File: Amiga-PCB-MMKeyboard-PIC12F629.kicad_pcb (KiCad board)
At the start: 2 copper layers, 47.3 x 23.2 mm, 13 parts, among them J11 Amiga keyboard, J12 A500 mainboard, J2 PS/2 keyboard, SW500 SW_Push, U1 PIC12F629

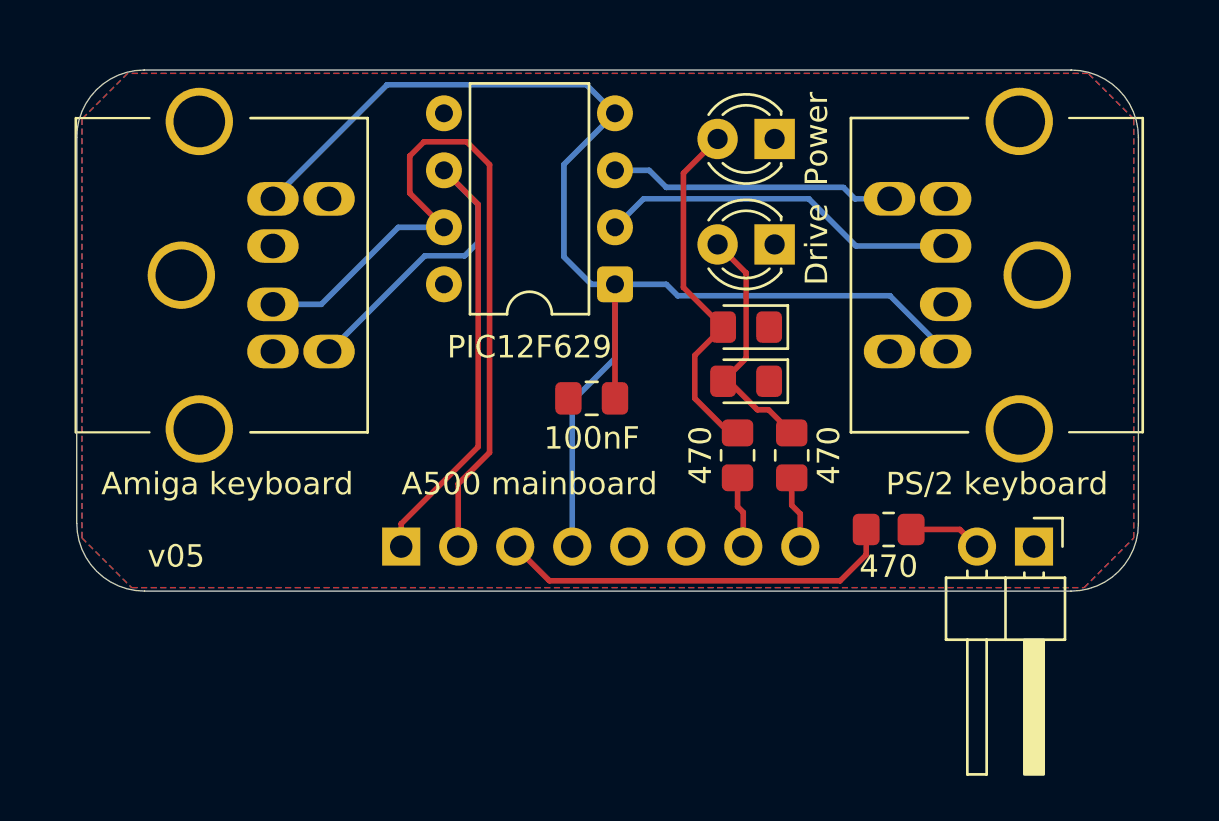
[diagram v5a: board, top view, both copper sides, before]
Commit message: v06: Sane LED resistor values depending on the LED's properties
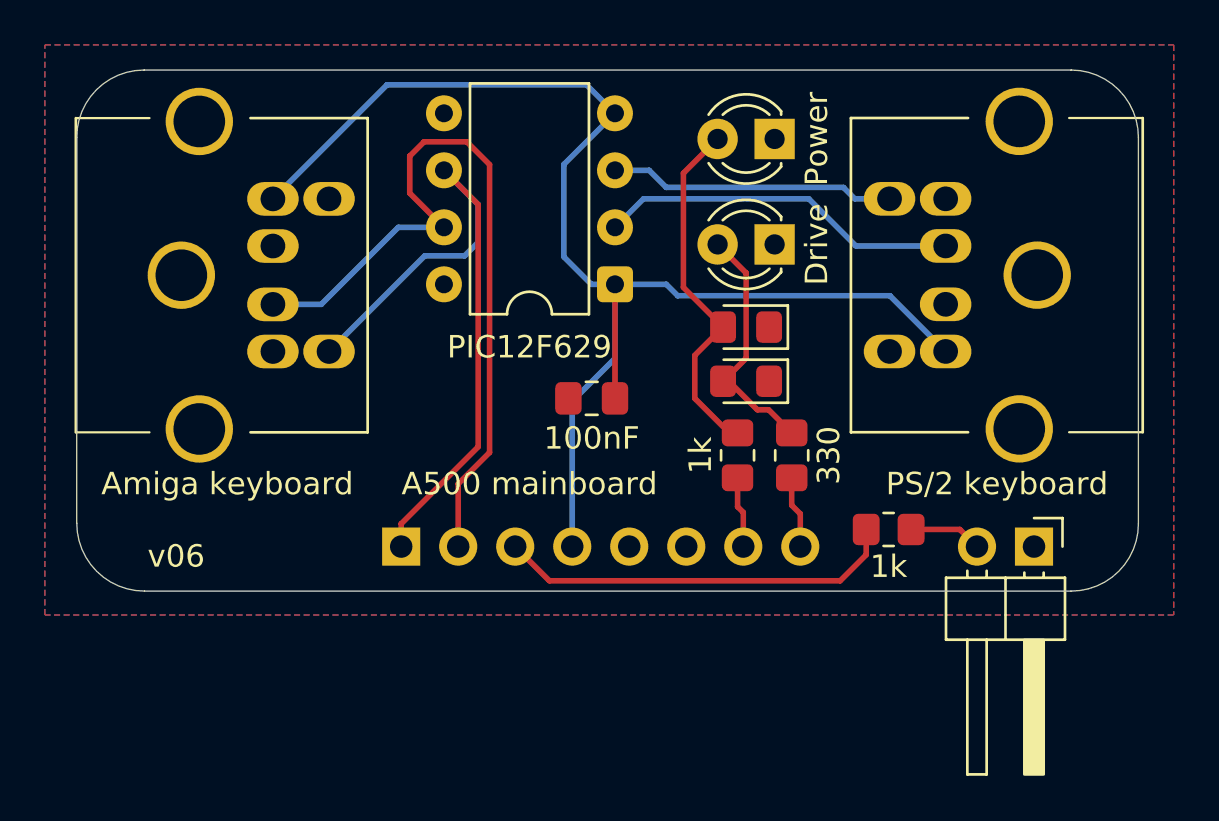
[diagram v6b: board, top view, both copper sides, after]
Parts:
- R1, R500: value 470 -> 1k
- R2: value 470 -> 330
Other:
- board text added: "v06"
- board text removed: "v05"
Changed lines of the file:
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@@
 			)
 		)
-		(property "Datasheet" ""
+		(property "Datasheet" "http://service.powerdynamics.com/ec/Catalog17/Section%2011.pdf"
 			(at 0 0 270)
 			(layer "F.Fab")
@@
 			)
 		)
-		(property "Description" "6-pin Mini-DIN connector"
+		(property "Description" ""
 			(at 0 0 270)
 			(layer "F.Fab")
@@
 			)
 		)
+		(property ki_fp_filters "MINI?DIN*")
+		(sheetname "/")
 		(sheetfile "Amiga-PCB-MMKeyboard-PIC12F629.kicad_sch")
 		(attr through_hole)
@@
 			)
 		)
-		(property "Description" "Light emitting diode"
+		(property "Description" ""
 			(at 0 0 180)
 			(layer "F.Fab")
@@
 			)
 		)
+		(property ki_fp_filters "LED* LED_SMD:* LED_THT:*")
+		(sheetname "/")
 		(sheetfile "Amiga-PCB-MMKeyboard-PIC12F629.kicad_sch")
 		(attr through_hole)
@@
 			)
 		)
-		(property "Value" "470"
+		(property "Value" "330"
 			(at 0 1.651 90)
 			(layer "F.SilkS")
@@
 			)
 		)
-		(property "Description" "Resistor"
+		(property "Description" ""
 			(at 0 0 90)
 			(layer "F.Fab")
@@
 			)
 		)
-		(property "JLCPCB" "C17710"
+		(property "JLCPCB" "C17630"
 			(at 243.586 -41.402 0)
 			(layer "F.Fab")
@@
 			)
 		)
-		(property "Reichelt" "SMD-0805 470"
+		(property "Reichelt" "SMD-0805 330"
 			(at 243.586 -41.402 0)
 			(layer "F.Fab")
@@
 			)
 		)
+		(property ki_fp_filters "R_*")
+		(sheetname "/")
 		(sheetfile "Amiga-PCB-MMKeyboard-PIC12F629.kicad_sch")
 		(attr smd)
@@
 			)
 		)
-		(property "Description" "Light emitting diode"
+		(property "Description" ""
 			(at 0 0 180)
 			(layer "F.Fab")
@@
 			)
 		)
+		(property ki_fp_filters "LED* LED_SMD:* LED_THT:*")
+		(sheetname "/")
 		(sheetfile "Amiga-PCB-MMKeyboard-PIC12F629.kicad_sch")
 		(attr smd)
@@
 			)
 		)
-		(property "Value" "470"
+		(property "Value" "1k"
 			(at 0 1.65 0)
 			(layer "F.SilkS")
@@
 			)
 		)
-		(property "Description" "Resistor"
+		(property "Description" ""
 			(at 0 0 0)
 			(layer "F.Fab")
@@
 			)
 		)
-		(property "JLCPCB" "C17710"
+		(property "JLCPCB" "C17513"
 			(at 0 0 0)
 			(layer "F.Fab")
@@
 			)
 		)
-		(property "Reichelt" "SMD-0805 470"
+		(property "Reichelt" "SMD-0805 1,00K"
 			(at 0 0 0)
 			(layer "F.Fab")
@@
 			)
 		)
+		(property ki_fp_filters "R_*")
+		(sheetname "/")
 		(sheetfile "Amiga-PCB-MMKeyboard-PIC12F629.kicad_sch")
 		(attr smd)
@@
 			)
 		)
-		(property "Description" "Push button switch, generic, two pins"
+		(property "Description" ""
 			(at 0 0 270)
 			(layer "F.Fab")
@@
 			)
 		)
+		(property "LCSC" "C7501290"
+			(at 0 0 270)
+			(unlocked yes)
+			(layer "F.Fab")
+			(hide yes)
+			(effects
+				(font
+					(size 1 1)
+					(thickness 0.15)
+				)
+			)
+		)
+		(property "Reichelt" "W+P 946-142"
+			(at 0 0 270)
+			(unlocked yes)
+			(layer "F.Fab")
+			(hide yes)
+			(effects
+				(font
+					(size 1 1)
+					(thickness 0.15)
+				)
+			)
+		)
+		(sheetname "/")
 		(sheetfile "Amiga-PCB-MMKeyboard-PIC12F629.kicad_sch")
 		(attr through_hole)
@@
 			)
 		)
-		(property "Datasheet" ""
+		(property "Datasheet" "http://ww1.microchip.com/downloads/en/DeviceDoc/41190G.pdf"
 			(at 0 0 180)
 			(layer "F.Fab")
@@
 			)
 		)
-		(property "Description" "1024W Flash, 64B SRAM, 128B EEPROM, PDIP8"
+		(property "Description" ""
 			(at 0 0 180)
 			(layer "F.Fab")
@@
 			)
 		)
+		(property ki_fp_filters "DIP*W7.62mm*")
+		(sheetname "/")
 		(sheetfile "Amiga-PCB-MMKeyboard-PIC12F629.kicad_sch")
 		(attr through_hole)
@@
 			)
 		)
-		(property "Description" "Light emitting diode"
+		(property "Description" ""
 			(at 0 0 180)
 			(layer "F.Fab")
@@
 			)
 		)
+		(property ki_fp_filters "LED* LED_SMD:* LED_THT:*")
+		(sheetname "/")
 		(sheetfile "Amiga-PCB-MMKeyboard-PIC12F629.kicad_sch")
 		(attr smd)
@@
 			)
 		)
-		(property "Datasheet" ""
+		(property "Datasheet" "http://service.powerdynamics.com/ec/Catalog17/Section%2011.pdf"
 			(at 0 0 90)
 			(layer "F.Fab")
@@
 			)
 		)
-		(property "Description" "6-pin Mini-DIN connector"
+		(property "Description" ""
 			(at 0 0 90)
 			(layer "F.Fab")
@@
 			)
 		)
+		(property ki_fp_filters "MINI?DIN*")
+		(sheetname "/")
 		(sheetfile "Amiga-PCB-MMKeyboard-PIC12F629.kicad_sch")
 		(attr through_hole)
@@
 			)
 		)
-		(property "Description" "Light emitting diode"
+		(property "Description" ""
 			(at 0 0 180)
 			(layer "F.Fab")
@@
 			)
 		)
+		(property ki_fp_filters "LED* LED_SMD:* LED_THT:*")
+		(sheetname "/")
 		(sheetfile "Amiga-PCB-MMKeyboard-PIC12F629.kicad_sch")
 		(attr through_hole)
@@
 			)
 		)
-		(property "Description" "Unpolarized capacitor"
+		(property "Description" ""
 			(at 0 0 180)
 			(layer "F.Fab")
@@
 			)
 		)
+		(property ki_fp_filters "C_*")
+		(sheetname "/")
 		(sheetfile "Amiga-PCB-MMKeyboard-PIC12F629.kicad_sch")
 		(attr smd)
@@
 			)
 		)
-		(property "Value" "470"
+		(property "Value" "1k"
 			(at -0.0019 -1.651 90)
 			(layer "F.SilkS")
@@
 			)
 		)
-		(property "Description" "Resistor"
+		(property "Description" ""
 			(at 0 0 90)
 			(layer "F.Fab")
@@
 			)
 		)
-		(property "JLCPCB" "C17710"
+		(property "JLCPCB" "C17513"
 			(at 241.1711 -38.9909 0)
 			(layer "F.Fab")
@@
 			)
 		)
-		(property "Reichelt" "SMD-0805 470"
+		(property "Reichelt" "SMD-0805 1,00K"
 			(at 241.1711 -38.9909 0)
 			(layer "F.Fab")
@@
 			)
 		)
+		(property ki_fp_filters "R_*")
+		(sheetname "/")
 		(sheetfile "Amiga-PCB-MMKeyboard-PIC12F629.kicad_sch")
 		(attr smd)
@@
 			)
 		)
-		(property "Description" "Generic connector, single row, 01x08, script generated"
+		(property "Description" ""
 			(at 0 0 270)
 			(layer "F.Fab")
@@
 			)
 		)
+		(property ki_fp_filters "Connector*:*_1x??_*")
+		(sheetname "/")
 		(sheetfile "Amiga-PCB-MMKeyboard-PIC12F629.kicad_sch")
 		(attr through_hole)
@@
 		(layer "Edge.Cuts")
 	)
-	(gr_text "v05"
+	(gr_text "v06"
 		(at 113.792 106.172 0)
 		(layer "F.SilkS")
@@
 		(polygon
 			(pts
-				(xy 110.871 86.106) (xy 110.871 104.775) (xy 113.0808 106.9848) (xy 155.5242 106.9848) (xy 157.734 104.775)
-				(xy 157.734 86.106) (xy 155.702 84.074) (xy 112.903 84.074)
+				(xy 109.22 82.804) (xy 159.512 82.804) (xy 159.512 108.204) (xy 109.22 108.204)
 			)
 		)
